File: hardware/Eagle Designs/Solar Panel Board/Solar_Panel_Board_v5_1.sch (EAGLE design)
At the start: 44 parts, among them J1 MOLEX_503763-0291MOLEX_503763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, J2 MOLEX_503763-0491MOLEX_503763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, J3 MOLEX_503763-0291MOLEX_503763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, U1 TMP36GSZ, U2 INA219BIDR

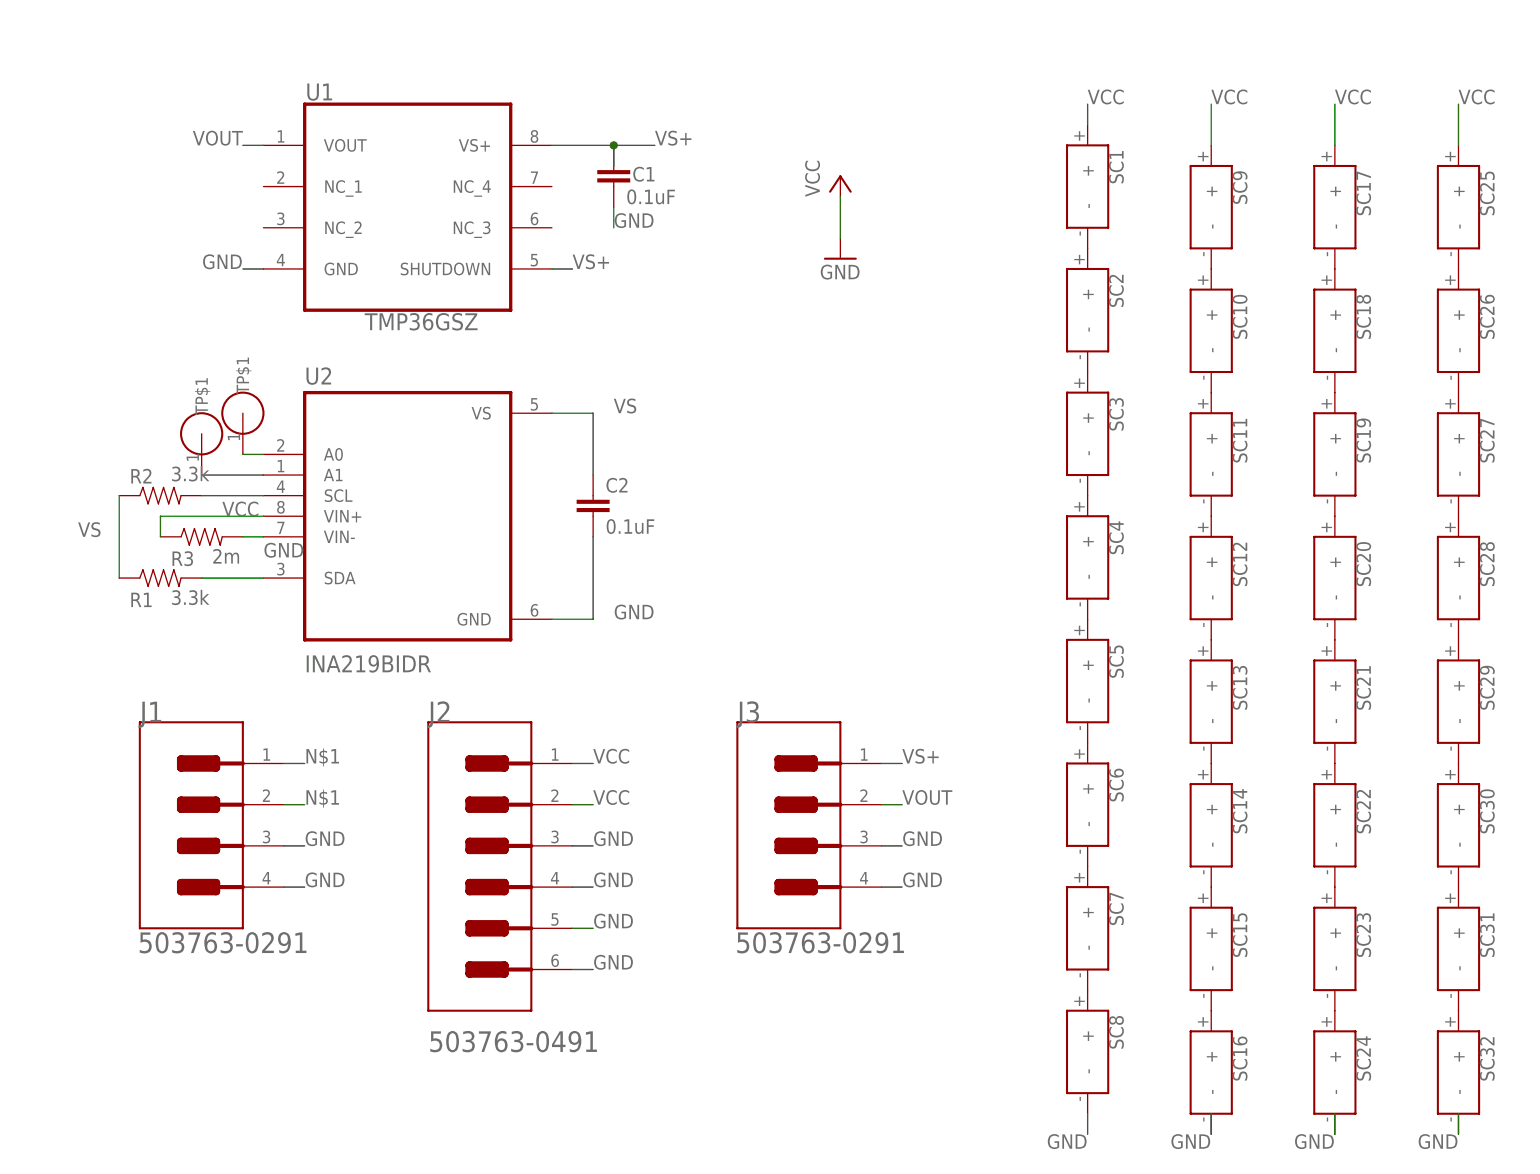
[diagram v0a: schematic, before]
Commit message: made improvements to the solar panel board and included cam outputs
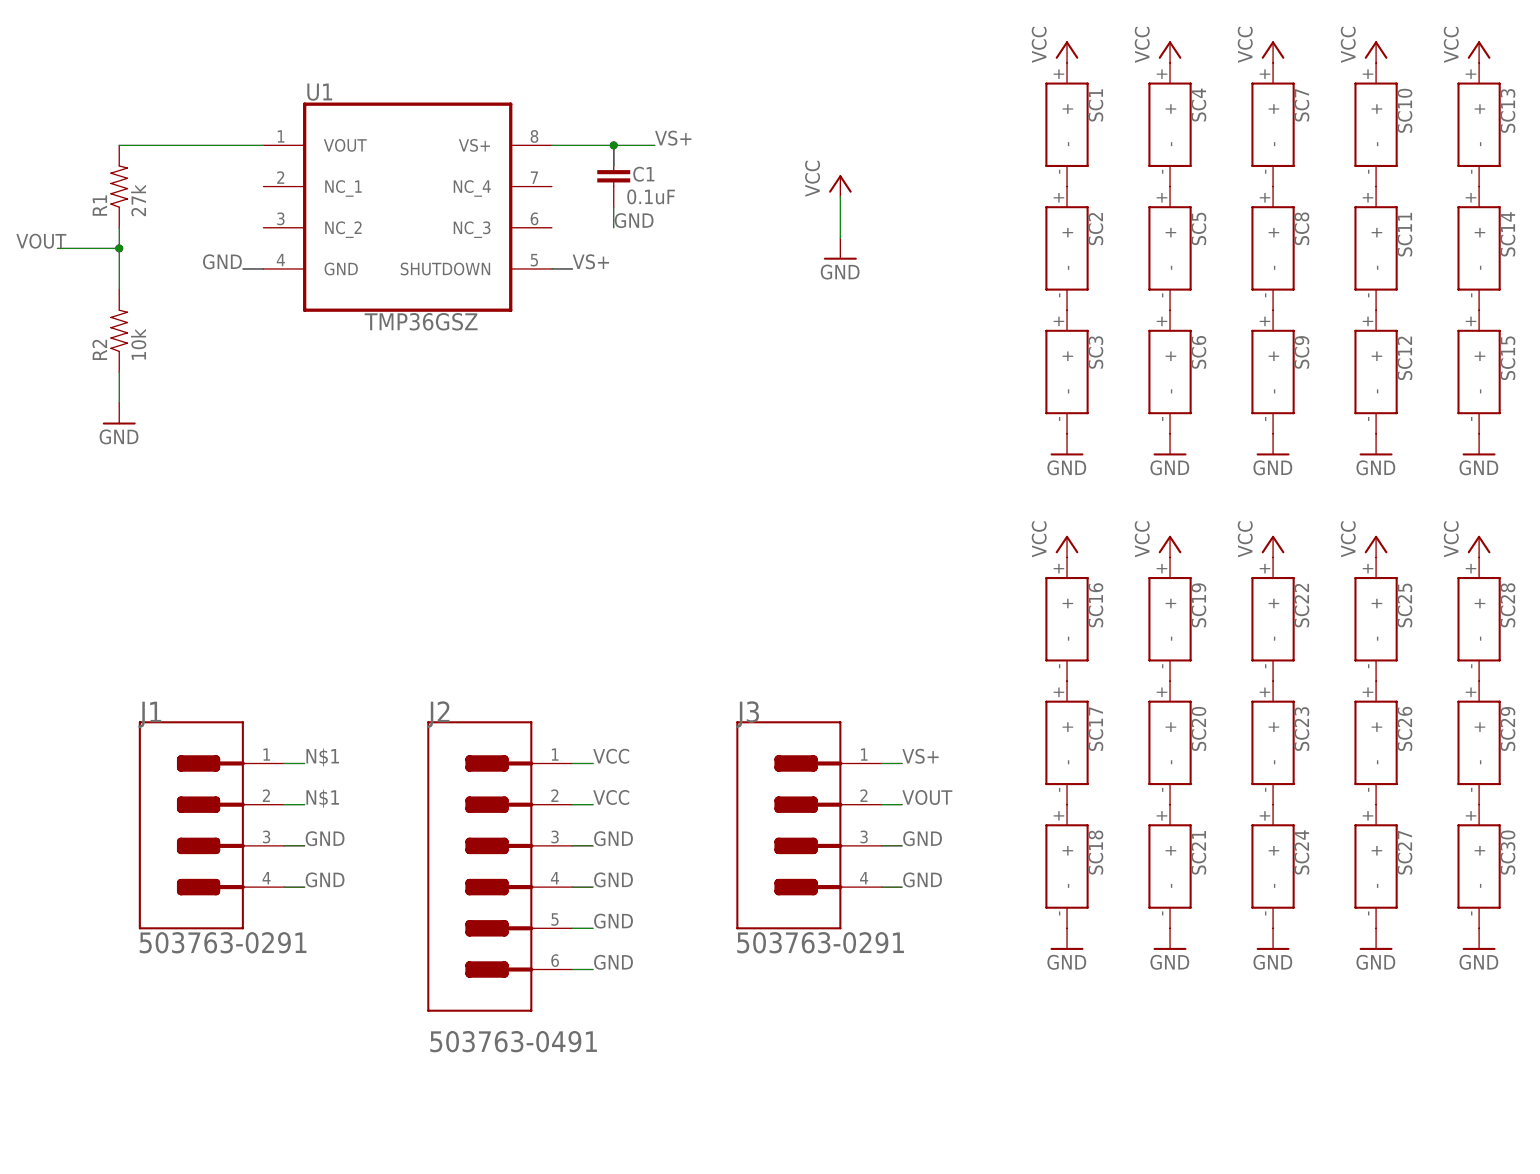
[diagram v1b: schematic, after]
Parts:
- removed C2: 0.1uF, HSFL_Main_Library:CAP0805
- removed R3: 2m, HSFL_Main_Library:RESISTOR0805-RES
- removed SC31, SC32: KXOB25-05X3F, untitled:KXOB25-05X3F
- removed U$1, U$2: TEST_POINT, HSFL_Main_Library:TEST_POINT
- removed U2: INA219BIDR, INA219BIDR:INA219BIDR
- R1: value 3.3k -> 27k
- R2: value 3.3k -> 10k
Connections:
- removed net N$16: SC21.-, SC22.+
- removed net N$17: SC18.-, SC19.+
- removed net N$20: SC31.-, SC32.+
- removed net N$25: SC27.-, SC28.+
- removed net N$31: U$1.TP$1, U2.A0
- removed net N$32: U$2.TP$1, U2.A1
- removed net N$33: R2.2, U2.SCL
- removed net N$36: R1.2, U2.SDA
- removed net VS: C2.1, R1.1, R2.1, U2.VS
- net GND: now also R2.1, SC12.-, SC15.-, SC18.-, SC21.-, SC27.-, SC3.-, SC30.-, SC6.-, SC9.-; no longer C2.2, R3.2, SC16.-, SC32.-, SC8.-, U2.GND, U2.VIN-
- net N$12: now also R1.2, U1.VOUT; no longer SC10.+, SC9.-
- net N$21: no longer SC30.-, SC31.+
- net N$3: no longer SC6.-, SC7.+
- net N$7: now also SC8.-, SC9.+; no longer SC3.-, SC4.+
- net N$8: now also SC16.-, SC17.+; no longer SC15.-, SC16.+
- net N$9: no longer SC12.-, SC13.+
- net VCC: now also SC10.+, SC13.+, SC16.+, SC19.+, SC22.+, SC28.+, SC4.+, SC7.+; no longer R3.1, SC17.+, SC9.+, U2.VIN+
- net VOUT: now also R1.1, R2.2; no longer U1.VOUT
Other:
- moved on the sheet: R1, R2, SC1, SC10, SC11, SC12, SC13, SC14, SC15, SC16, SC17, SC18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
